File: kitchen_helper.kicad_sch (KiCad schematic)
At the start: 45 parts, among them IC1 ESP32-S3-WROOM-1-N8R8, IC2 FS312F-G, IC3 3v3 Regulator, J1 Bat+, J2 PROG_HDR, J3 DISP_HDR, J4 Temp 1, J5 Temp 2, J6 GND, J7 Battery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

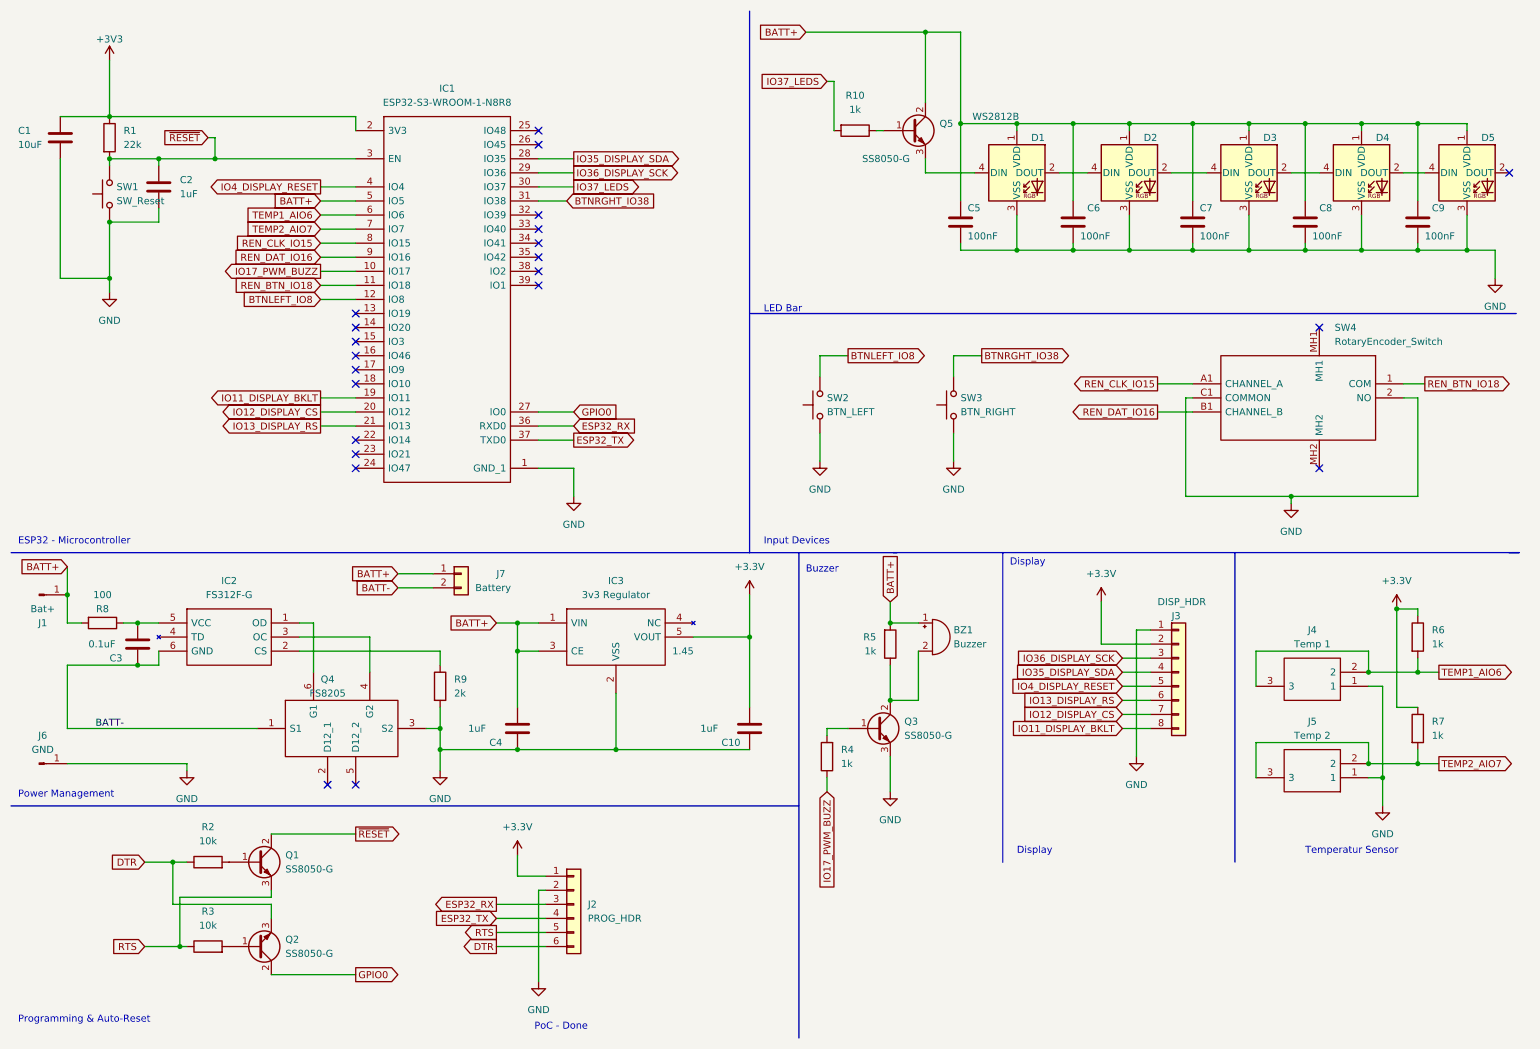
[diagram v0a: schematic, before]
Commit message: Modifications for ADC ports
- Changed voltage divider resistor to 100k
- Changed the voltage supply for the ADC pins from 3v3 to a GPIO Pin to turn them on only as needeed.
- Deleted some old files
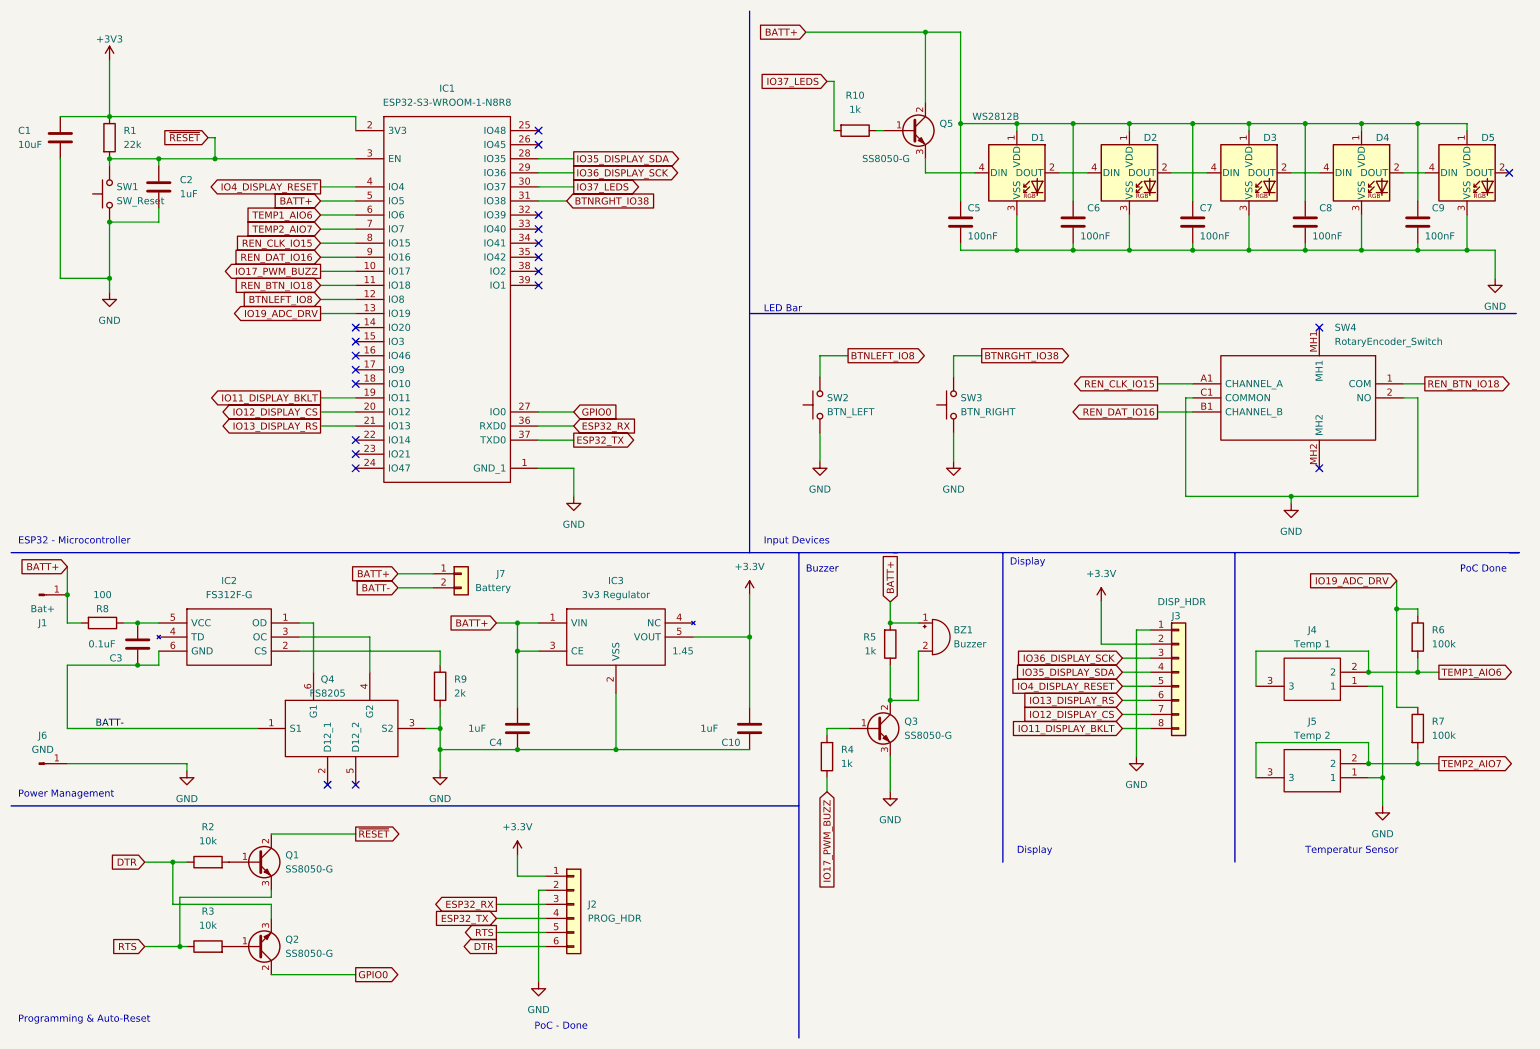
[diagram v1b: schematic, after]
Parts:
- R6, R7: value 1k -> 100k
- R9: footprint (none) -> Resistor_SMD:R_0603_1608Metric_Pad0.98x0.95mm_HandSolder
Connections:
- net +3V3: no longer R6.1, R7.1
- net IO19_ADC_DRV: now reaches IC1.13 (IO19)
- net IO19_ADC_DRV: now also R6.1, R7.1
- no-connect marks 22 -> 21
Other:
- note added: "PoC Done"
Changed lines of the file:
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@@
   (junction (at 121.92 146.05) (diameter 0) (color 0 0 0 0)
   )
+  (junction (at 262.89 120.65) (diameter 0) (color 0 0 0 0)
+  )
   (junction (at 246.38 33.02) (diameter 0) (color 0 0 0 0)
   )
   (junction (at 171.45 123.19) (diameter 0) (color 0 0 0 0)
   )
-  (junction (at 262.89 120.65) (diameter 0) (color 0 0 0 0)
-  )
   (junction (at 90.17 146.05) (diameter 0) (color 0 0 0 0)
   )
@@
   )
   (no_connect (at 74.93 74.93))
-  (no_connect (at 74.93 67.31))
   (no_connect (at 74.93 69.85))
   (no_connect (at 74.93 90.17))
@@
     (stroke (width 0) (type default) (color 0 0 0 0))
   )
+  (wire (pts (xy 68.58 67.31) (xy 74.93 67.31))
+    (stroke (width 0) (type default) (color 0 0 0 0))
+  )
   (wire (pts (xy 243.84 101.6) (xy 243.84 100.33))
     (stroke (width 0) (type default) (color 0 0 0 0))
@@
     (stroke (width 0) (type default) (color 0 0 0 0))
   )
+  (wire (pts (xy 262.89 115.57) (xy 262.89 120.65))
+    (stroke (width 0) (type default) (color 0 0 0 0))
+  )
   (wire (pts (xy 59.69 171.45) (xy 59.69 172.72))
     (stroke (width 0) (type default) (color 0 0 0 0))
@@
   )
   (text "Input Devices" (at 148.59 109.22 0)
+    (effects (font (size 1.27 1.27)) (justify left bottom))
+  )
+  (text "PoC Done" (at 274.32 114.3 0)
     (effects (font (size 1.27 1.27)) (justify left bottom))
   )
@@
     )
   )
+  (global_label "IO19_ADC_DRV" (shape input) (at 262.89 115.57 180) (fields_autoplaced)
+    (effects (font (size 1.27 1.27)) (justify right))
+    (property "Intersheet References" "${INTERSHEET_REFS}" (id 0) (at 247.0191 115.4906 0)
+      (effects (font (size 1.27 1.27)) (justify right) hide)
+    )
+  )
   (global_label "DTR" (shape input) (at 36.83 166.37 180) (fields_autoplaced)
     (effects (font (size 1.27 1.27)) (justify right))
@@
     )
   )
+  (global_label "IO19_ADC_DRV" (shape output) (at 68.58 67.31 180) (fields_autoplaced)
+    (effects (font (size 1.27 1.27)) (justify right))
+    (property "Intersheet References" "${INTERSHEET_REFS}" (id 0) (at 52.7091 67.2306 0)
+      (effects (font (size 1.27 1.27)) (justify right) hide)
+    )
+  )
   (global_label "IO37_LEDS" (shape input) (at 160.02 25.4 180) (fields_autoplaced)
     (effects (font (size 1.27 1.27)) (justify right))
@@
       (effects (font (size 1.27 1.27)) (justify left))
     )
-    (property "Value" "1k" (id 1) (at 269.24 126.9999 0)
+    (property "Value" "100k" (id 1) (at 269.24 126.9999 0)
       (effects (font (size 1.27 1.27)) (justify left))
     )
@@
       (effects (font (size 1.27 1.27)) (justify left))
     )
-    (property "Value" "1k" (id 1) (at 269.24 143.5099 0)
+    (property "Value" "100k" (id 1) (at 269.24 143.5099 0)
       (effects (font (size 1.27 1.27)) (justify left))
     )
@@
       (effects (font (size 1.27 1.27)) (justify left))
     )
-    (property "Footprint" "" (id 2) (at 88.392 134.62 90)
+    (property "Footprint" "Resistor_SMD:R_0603_1608Metric_Pad0.98x0.95mm_HandSolder" (id 2) (at 88.392 134.62 90)
       (effects (font (size 1.27 1.27)) hide)
     )
@@
     (pin "2")
   )
-  (symbol (lib_id "power:+3.3V") (at 262.89 120.65 0) (unit 1)
-    (in_bom yes) (on_board yes) (fields_autoplaced)
-    (property "Reference" "#PWR0117" (id 0) (at 262.89 124.46 0)
-      (effects (font (size 1.27 1.27)) hide)
-    )
-    (property "Value" "+3.3V" (id 1) (at 262.89 115.57 0))
-    (property "Footprint" "" (id 2) (at 262.89 120.65 0)
-      (effects (font (size 1.27 1.27)) hide)
-    )
-    (property "Datasheet" "" (id 3) (at 262.89 120.65 0)
-      (effects (font (size 1.27 1.27)) hide)
-    )
-    (pin "1")
-  )
   (symbol (lib_id "Li-Ion Charging:FS312F-G") (at 39.37 123.19 0) (unit 1)
     (in_bom yes) (on_board yes) (fields_autoplaced)
@@
       (reference "#PWR0116") (unit 1) (value "GND") (footprint "")
     )
-    (path "/ccd46195-be18-4e89-b582-37934d69ebc0"
-      (reference "#PWR0117") (unit 1) (value "+3.3V") (footprint "")
-    )
     (path "/f0a65704-ae0b-45cb-9d23-045c843125a2"
       (reference "#PWR0118") (unit 1) (value "GND") (footprint "")
@@
     )
     (path "/29498119-4e01-42ca-958c-2423de5efa86"
-      (reference "R6") (unit 1) (value "1k") (footprint "Resistor_SMD:R_0603_1608Metric_Pad0.98x0.95mm_HandSolder")
+      (reference "R6") (unit 1) (value "100k") (footprint "Resistor_SMD:R_0603_1608Metric_Pad0.98x0.95mm_HandSolder")
     )
     (path "/9701cc8f-6483-4e59-bb9d-470df771c239"
-      (reference "R7") (unit 1) (value "1k") (footprint "Resistor_SMD:R_0603_1608Metric_Pad0.98x0.95mm_HandSolder")
+      (reference "R7") (unit 1) (value "100k") (footprint "Resistor_SMD:R_0603_1608Metric_Pad0.98x0.95mm_HandSolder")
     )
     (path "/fc4979bc-90fd-4e01-aeea-a0d9fffb5b6a"

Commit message: Corrected issues found during schematic verification
- splitted driving lines for both temperature sensors to prevent nfluencing through parallel resistance
- swaped the two directions of the rotary encoder
- Powering the TFT backlight from BATT+ as the voltage drop at the resistor is too much for 3v3
- Added resistor network to directly pull rotary encorder to 3v3
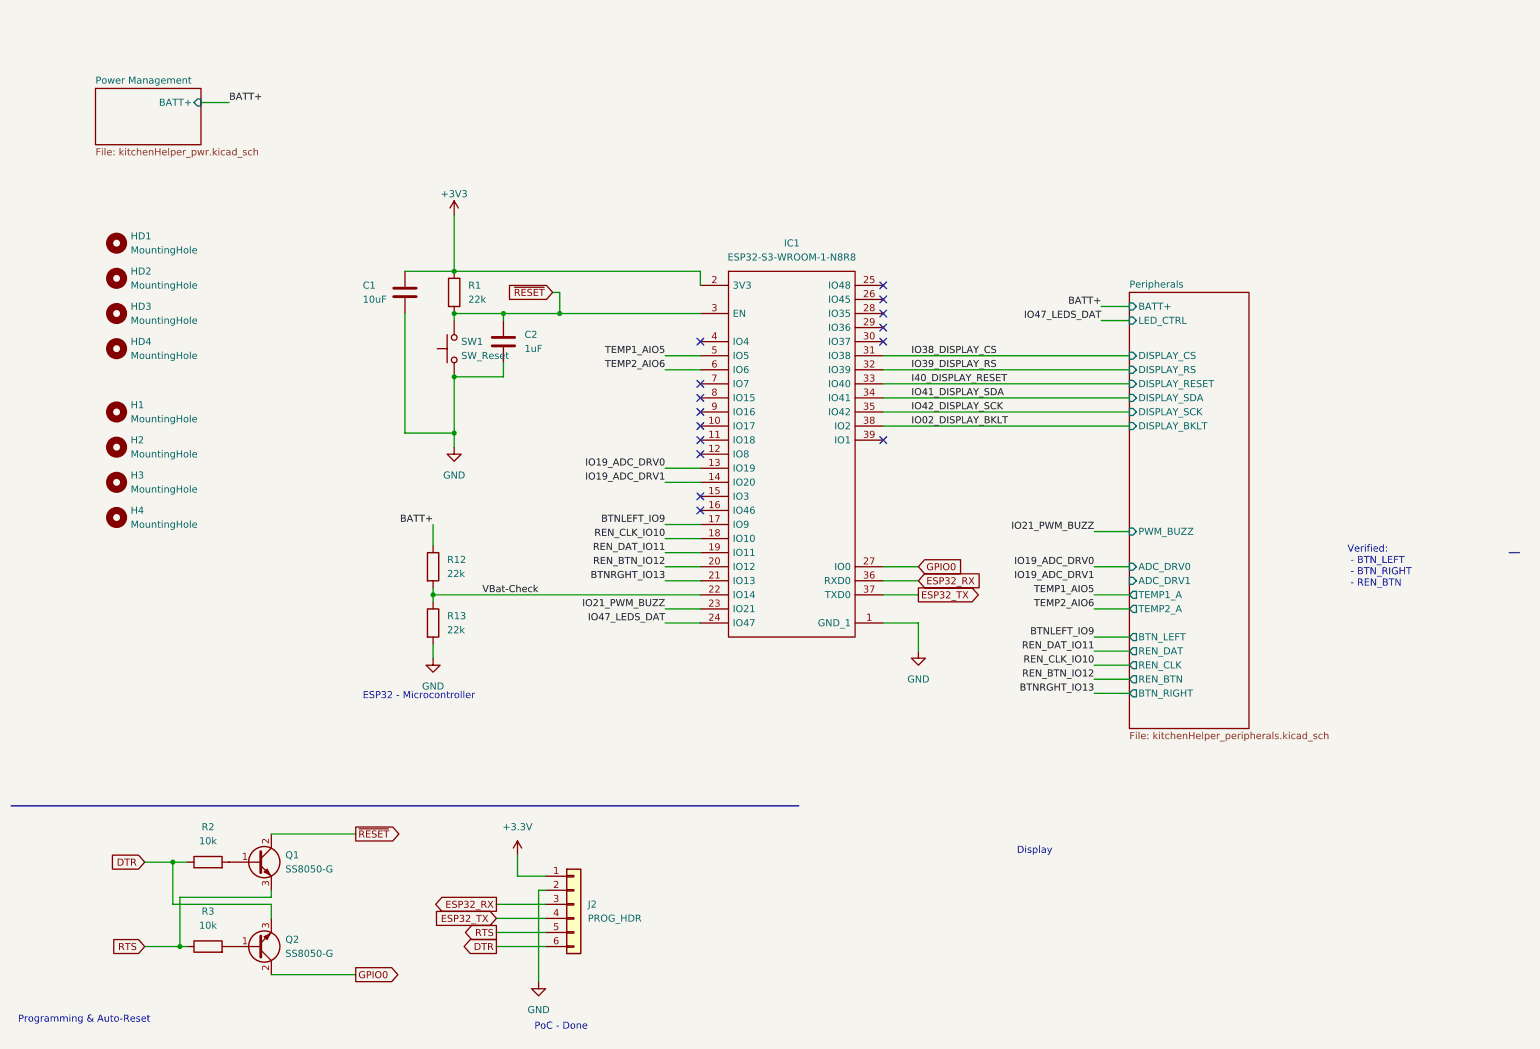
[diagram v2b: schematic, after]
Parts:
- removed BZ1: Buzzer, footprints:PS1240P02BT, symbol Device:Buzzer
- removed C10, C4: 1uF, Capacitor_SMD:C_0603_1608Metric_Pad1.08x0.95mm_HandSolder, symbol Device:C
- removed C3: 0.1uF, Capacitor_SMD:C_0603_1608Metric_Pad1.08x0.95mm_HandSolder, symbol Device:C
- removed C5, C6, C7, C8, C9: 100nF, Capacitor_SMD:C_0603_1608Metric_Pad1.08x0.95mm_HandSolder, symbol Device:C
- removed D1, D2, D3, D4, D5: WS2812B, LED_SMD:LED_WS2812B_PLCC4_5.0x5.0mm_P3.2mm, symbol LED:WS2812B
- removed IC2: FS312F-G, footprints:SOT95P280X145-6N, symbol Li-Ion Charging:FS312F-G
- removed IC3: 3v3 Regulator, footprints:SOT95P270X145-5N, symbol Regulator_Linear:ME6211C33M5G-N
- removed J1: Bat+, Connector_Wire:SolderWirePad_1x01_SMD+Via_2x3mm, symbol Connector:Conn_01x01_Male
- removed J3: DISP_HDR, Connector_PinHeader_2.54mm:PinHeader_1x08_P2.54mm_Vertical, symbol Connector_Generic:Conn_01x08
- removed J4: Temp 1, footprints:MJ2509N, symbol MJ-2509N:MJ-2509N
- removed J5: Temp 2, footprints:MJ2509N, symbol MJ-2509N:MJ-2509N
- removed J6: GND, Connector_Wire:SolderWirePad_1x01_SMD+Via_2x3mm, symbol Connector:Conn_01x01_Male
- removed J7: Battery, Connector_PinHeader_2.54mm:PinHeader_1x02_P2.54mm_Vertical, symbol Connector_Generic:Conn_01x02
- removed Q3, Q5: SS8050-G, Package_TO_SOT_SMD:SOT-23, symbol Device:Q_NPN_BCE
- removed Q4: FS8205, footprints:FS8205, symbol FS8205:FS8205
- removed R10, R4, R5: 1k, Resistor_SMD:R_0603_1608Metric_Pad0.98x0.95mm_HandSolder, symbol Device:R
- removed R6, R7: 100k, Resistor_SMD:R_0603_1608Metric_Pad0.98x0.95mm_HandSolder, symbol Device:R
- removed R8: 100, Resistor_SMD:R_0603_1608Metric_Pad0.98x0.95mm_HandSolder, symbol Device:R
- removed R9: 2k, Resistor_SMD:R_0603_1608Metric_Pad0.98x0.95mm_HandSolder, symbol Device:R
- removed SW2: BTN_LEFT, Button_Switch_THT:SW_PUSH_6mm, symbol Switch:SW_Push
- removed SW3: BTN_RIGHT, Button_Switch_THT:SW_PUSH_6mm, symbol Switch:SW_Push
- removed SW4: RotaryEncoder_Switch, footprints:PEC12R3120FS0012, symbol PEC12R-3120F-S0012:PEC12R-3120F-S0012
- added H1, H2, H3, H4: MountingHole, MountingHole:MountingHole_3mm_Pad, symbol Mechanical:MountingHole
- added HD1, HD2, HD3, HD4: MountingHole, MountingHole:MountingHole_3.2mm_M3, symbol Mechanical:MountingHole
- added R12, R13: 22k, Resistor_SMD:R_0603_1608Metric_Pad0.98x0.95mm_HandSolder, symbol Device:R
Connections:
- net BATT+: now also R12.1; no longer IC1.5 (IO5)
- net GND: now also R13.2
- net IO19_ADC_DRV1: now reaches IC1.14 (IO20)
- net BTNLEFT_IO9: now reaches IC1.17 (IO9)
- net REN_CLK_IO10: now reaches IC1.18 (IO10)
- net VBat-Check: now reaches IC1.22 (IO14)
- net VBat-Check: now also R12.2, R13.1
- net IO21_PWM_BUZZ: now reaches IC1.23 (IO21)
- net IO47_LEDS_DAT: now reaches IC1.24 (IO47)
- net IO39_DISPLAY_RS: now reaches IC1.32 (IO39)
- net I40_DISPLAY_RESET: now reaches IC1.33 (IO40)
- net IO41_DISPLAY_SDA: now reaches IC1.34 (IO41)
- net IO42_DISPLAY_SCK: now reaches IC1.35 (IO42)
- net IO02_DISPLAY_BKLT: now reaches IC1.38 (IO2)
- net BTNLEFT_IO8: no longer names the net of IC1.12 (IO8)
- net BTNRGHT_IO38 renamed IO38_DISPLAY_CS
- net IO11_DISPLAY_BKLT renamed REN_DAT_IO11
- net IO12_DISPLAY_CS renamed REN_BTN_IO12
- net IO13_DISPLAY_RS renamed BTNRGHT_IO13
- net IO17_PWM_BUZZ: no longer names the net of IC1.10 (IO17)
- net IO19_ADC_DRV renamed IO19_ADC_DRV0
- net IO35_DISPLAY_SDA: no longer names the net of IC1.28 (IO35)
- net IO36_DISPLAY_SCK: no longer names the net of IC1.29 (IO36)
- net IO37_LEDS: no longer names the net of IC1.30 (IO37)
- net IO4_DISPLAY_RESET: no longer names the net of IC1.4 (IO4)
- net REN_BTN_IO18: no longer names the net of IC1.11 (IO18)
- net REN_CLK_IO15: no longer names the net of IC1.8 (IO15)
- net REN_DAT_IO16: no longer names the net of IC1.9 (IO16)
- net TEMP1_AIO6 renamed TEMP2_AIO6
- net TEMP2_AIO7: no longer names the net of IC1.7 (IO7)
- new net TEMP1_AIO5: IC1.5 (IO5)
- no-connect marks 21 -> 15
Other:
- added sheet Peripherals (kitchenHelper_peripherals.kicad_sch)
- added sheet Power Management (kitchenHelper_pwr.kicad_sch)
- note added: "Verified: - BTN_LEFT - BTN_RIGHT - REN_BTN"
- note removed: "Buzzer"
- note removed: "Input Devices"
- note removed: "LED Bar"
- note removed: "PoC Done"
- note removed: "Power Management"
- note removed: "Temperatur Sensor"
- moved on the sheet: C1, C2, IC1, R1, SW1
